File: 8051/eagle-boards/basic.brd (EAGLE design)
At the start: 65.7 x 76.2 mm, 29 parts, among them IC1 AT89S51-24P, IC2 ULN2003AN, IC3 ULN2003AN, Q1 12M

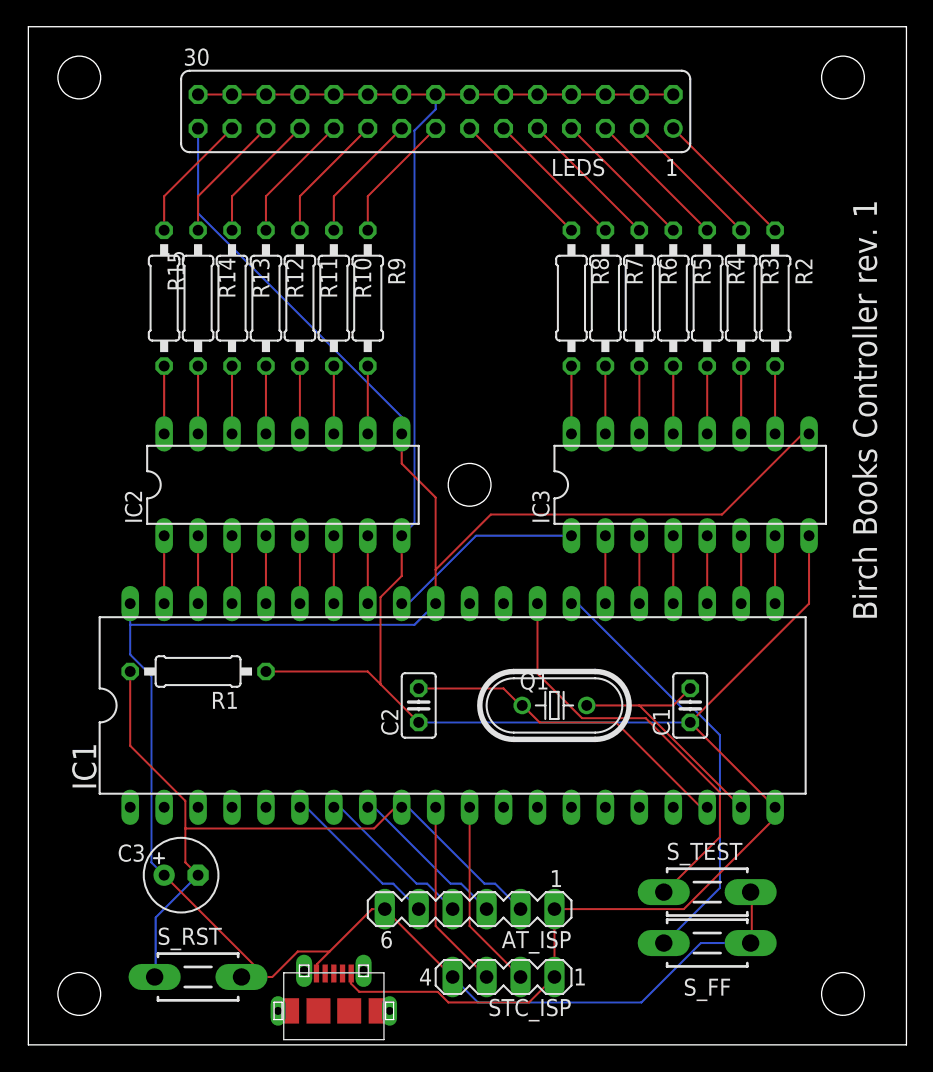
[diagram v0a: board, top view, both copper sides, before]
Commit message: Split the actuation into its own board.
Note that the previous design was broken, as the Darlingtons weren't being grounded, but rather joined to Vcc.
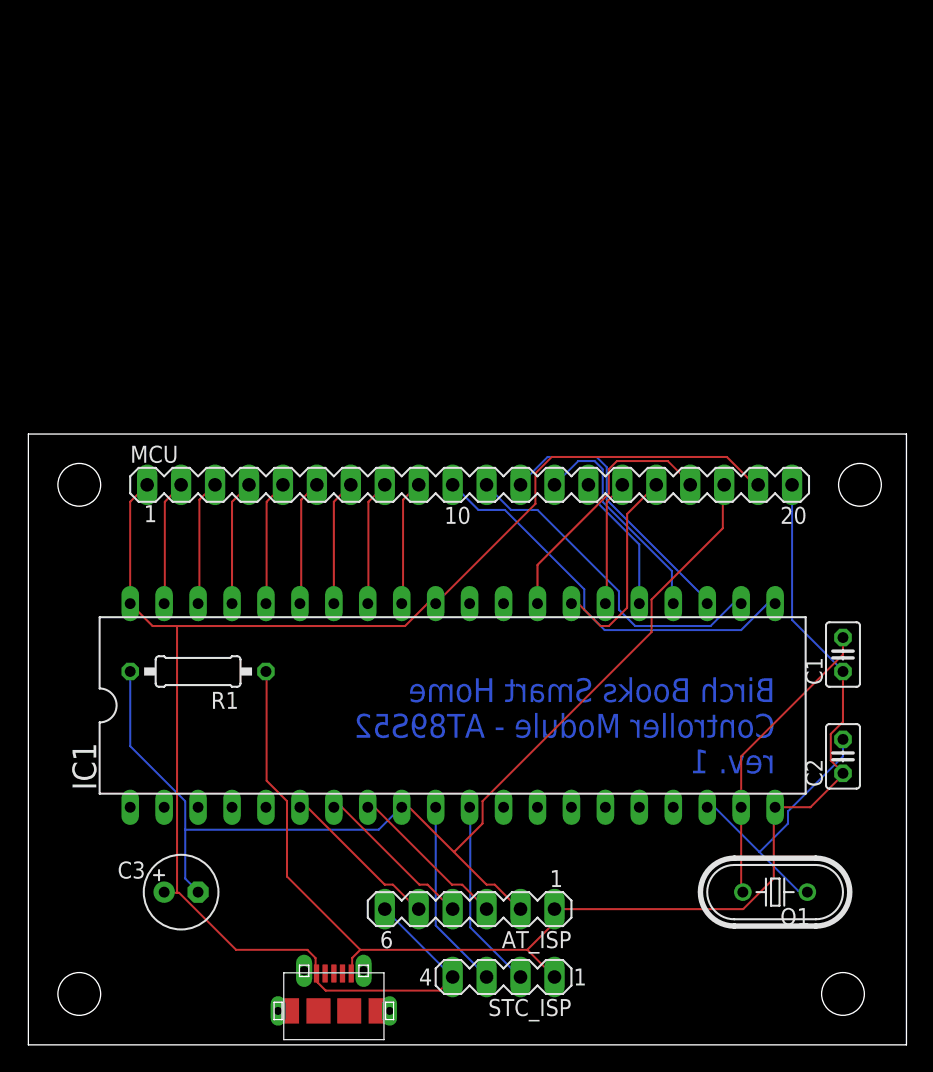
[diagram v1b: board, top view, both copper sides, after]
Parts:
- removed IC2, IC3: ULN2003AN, uln-udn:DIL16
- removed LEDS: (no value), con-lsta:FE15-2
- removed R10, R11, R12, R13, R14, R15, R2, R3, R4, R5, R6, R7, R8, R9: 47, rcl:0207/10
- removed S_FF, S_RST, S_TEST: DTS-3, switch-tact:DTS-3
- added MCU: (no value), con-lstb:MA20-1
- moved C2 32.0 mm to (61.0, 19.1)
- moved Q1 21.6 mm to (55.9, 8.89), turned to 180 degrees
- moved C1 12.0 mm to (61.0, 26.7)
- moved C3 1.27 mm to (11.4, 8.89)
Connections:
- removed net N$21: IC3.11, R3.2
- removed net N$22: IC3.12, R4.2
- removed net N$23: IC3.13, R5.2
- removed net N$24: IC3.14, R6.2
- removed net N$25: IC3.15, R7.2
- removed net N$26: IC3.16, R8.2
- removed net N$27: IC2.10, R9.2
- removed net N$28: IC2.11, R10.2
- removed net N$29: IC2.12, R11.2
- removed net N$30: IC2.13, R12.2
- removed net N$31: IC2.14, R13.2
- removed net N$32: IC2.15, R14.2
- removed net N$33: IC2.16, R15.2
- removed net N$34: LEDS.27, R15.1
- removed net N$35: LEDS.25, R14.1
- removed net N$36: LEDS.23, R13.1
- removed net N$37: LEDS.21, R12.1
- removed net N$38: LEDS.19, R11.1
- removed net N$39: LEDS.17, R10.1
- removed net N$40: LEDS.15, R9.1
- removed net N$41: LEDS.13, R8.1
- removed net N$42: LEDS.11, R7.1
- removed net N$43: LEDS.9, R6.1
- removed net N$44: LEDS.7, R5.1
- removed net N$45: LEDS.5, R4.1
- removed net N$46: LEDS.3, R3.1
- removed net N$47: LEDS.1, R2.1
- removed net N$48: IC1.28, S_TEST.1
- net GND: now also MCU.20; no longer IC2.8, IC3.8, LEDS.10, LEDS.12, LEDS.14, LEDS.16, LEDS.18, LEDS.2, LEDS.20, LEDS.22, LEDS.24, LEDS.26, LEDS.28, LEDS.30, LEDS.4, LEDS.6, LEDS.8
- net N$1: now also IC1.39, MCU.2; no longer IC1.21, IC3.7
- net N$10: now also IC1.33, MCU.8; no longer IC1.35, IC2.5
- net N$11: now also IC1.32, MCU.9; no longer IC1.34, IC2.6
- net N$12: now also IC1.21, MCU.10; no longer IC1.33, IC2.7
- net N$13: now also IC1.22, MCU.11; no longer IC1.32, IC3.1
- net N$14: now also MCU.12; no longer IC3.5
- net N$15: now also MCU.13; no longer IC3.4
- net N$16: now also MCU.14; no longer IC3.3
- net N$17: now also MCU.15; no longer IC3.2
- net N$19: now also MCU.16; no longer S_FF.1
- net N$2: now also IC1.38, MCU.3; no longer IC1.22, IC3.6
- net N$20: now also IC1.28, MCU.17; no longer IC3.10, R2.2
- net N$5: now also MCU.18; no longer S_RST.1
- net N$6: now also IC1.37, MCU.4; no longer IC1.39, IC2.1
- net N$7: now also IC1.36, MCU.5; no longer IC1.38, IC2.2
- net N$8: now also IC1.35, MCU.6; no longer IC1.37, IC2.3
- net N$9: now also IC1.34, MCU.7; no longer IC1.36, IC2.4
- net VCC: now also MCU.1, MCU.19; no longer IC2.9, IC3.9, LEDS.29, S_FF.2, S_RST.2, S_TEST.2
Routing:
- net GND: track 183.9 -> 98.0 mm
- net VCC: track 181.7 -> 117.8 mm
- net N$48: track 31.8 -> 0.00 mm
- net N$5: track 55.3 -> 83.4 mm
- net N$12: track 5.08 -> 30.3 mm
- net N$19: track 32.5 -> 15.5 mm
- net N$14: track 5.08 -> 21.0 mm
- net N$20: track 5.08 -> 19.4 mm
- net N$15: track 5.08 -> 16.9 mm
- net N$47: track 10.8 -> 0.00 mm
- net N$46: track 10.8 -> 0.00 mm
- net N$45: track 10.8 -> 0.00 mm
- net N$44: track 10.8 -> 0.00 mm
- net N$43: track 10.8 -> 0.00 mm
- net N$42: track 10.8 -> 0.00 mm
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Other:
- board size 65.7 x 76.2 mm -> 65.7 x 45.7 mm
- board text added: "Birch Books Smart Home Controller Module - AT89S52 rev. 1"
- board text removed: "Birch Books Controller rev. 1"

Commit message: Fix significant mistakes in the controller board.
The capacitors to stabilise the crystal need to be a bit beefier, make space for them.

Replace the pin header with a female header for the connection to the actuator board.

Necessary: add a resistor network between P0 and the connector.

P0 is the only port needing pull-up resistors.
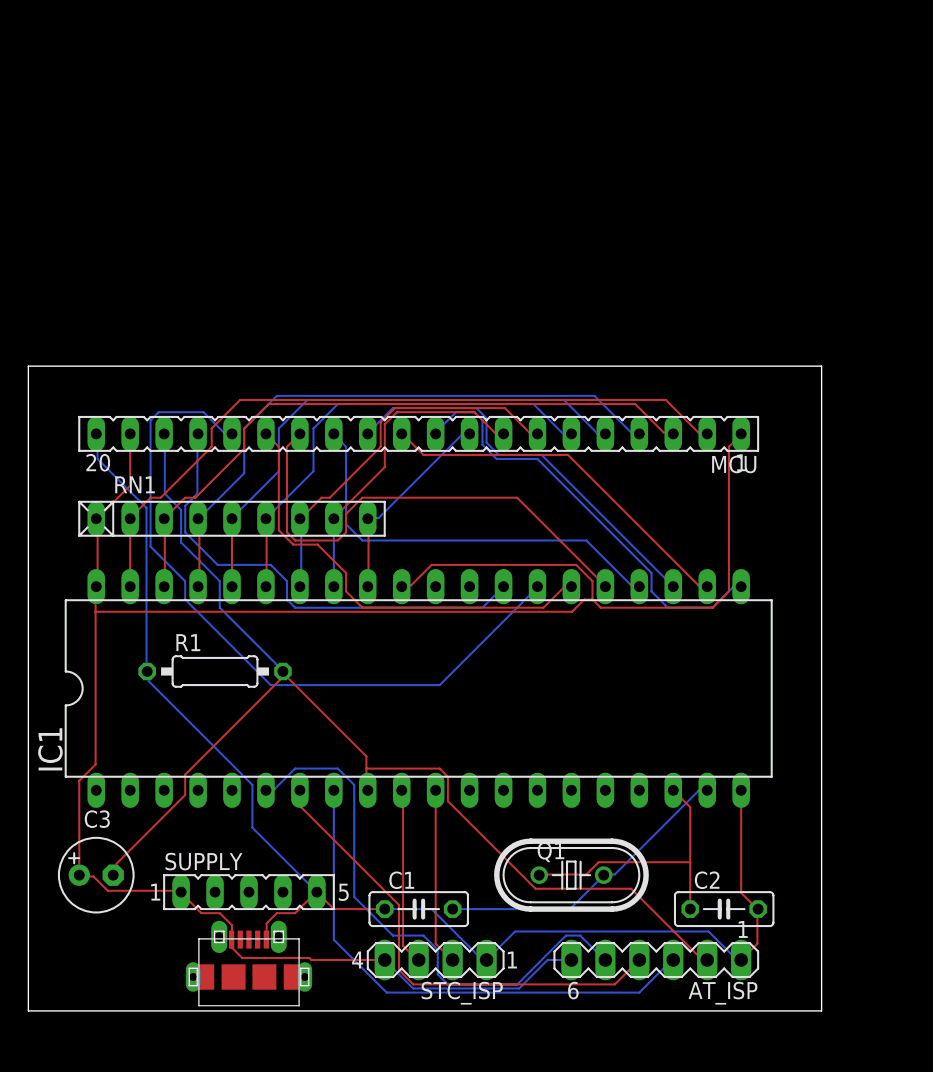
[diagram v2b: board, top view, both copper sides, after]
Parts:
- added RN1: 10k, resistor-net:RN-9
- added SUPPLY: (no value), con-lsta:FE05-1
- C1, C2: value 22p -> 50pF; device rcl:C025-025X050 -> rcl:C050-025X075
- MCU: device con-lstb:MA20-1 -> con-lsta:FE20
- moved C1 37.0 mm to (29.2, 7.62), turned to 0 degrees
- moved Q1 15.3 mm to (40.6, 10.2), turned to 0 degrees
- moved C2 14.5 mm to (52.1, 7.62), turned to 180 degrees
- moved AT_ISP 14.5 mm to (47.0, 3.81)
- moved U$1 6.84 mm to (16.5, 2.54)
- moved C3 6.48 mm to (5.08, 10.2)
- moved MCU 5.39 mm to (29.2, 43.2), turned to 180 degrees
- moved STC_ISP 5.24 mm to (30.5, 3.81)
- moved IC1 2.84 mm to (29.2, 24.1)
- moved R1 1.27 mm to (14.0, 25.4), turned to 0 degrees
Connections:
- removed net N$1: IC1.39, MCU.2
- removed net N$2 (its old number): IC1.38, MCU.3
- removed net N$6 (its old number): IC1.37, MCU.4
- removed net N$8 (its old number): IC1.35, MCU.6
- removed net N$9 (its old number): IC1.34, MCU.7
- new net N$12: IC1.34, MCU.7, RN1.7
- new net N$13: IC1.33, MCU.8, RN1.8
- new net N$14: IC1.32, MCU.9, RN1.9
- new net N$22: IC1.37, MCU.4, RN1.4
- new net N$26: IC1.39, MCU.2, RN1.2
- net GND: now also SUPPLY.5
- net N$10: now also IC1.36, MCU.5, RN1.5; no longer IC1.33, MCU.8
- net N$11: now also IC1.35, MCU.6, RN1.6; no longer IC1.32, MCU.9
- net N$7: now also IC1.38, MCU.3, RN1.3; no longer IC1.36, MCU.5
- net VCC: now also RN1.1, SUPPLY.1
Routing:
- net N$26: track 0.00 -> 53.8 mm
- net N$22: track 0.00 -> 45.2 mm
- net N$7: track 9.45 -> 48.6 mm
- net N$6: track 15.5 -> 53.7 mm
- net VCC: track 117.8 -> 154.6 mm
- net N$10: track 9.45 -> 39.7 mm
- net N$51: track 12.0 -> 41.0 mm
- net N$12: track 0.00 -> 28.3 mm
- net N$49: track 12.0 -> 39.2 mm
- net N$9: track 10.5 -> 36.7 mm
- net N$11: track 9.50 -> 34.3 mm
- net N$8: track 9.52 -> 33.4 mm
- net N$50: track 12.0 -> 35.7 mm
- net N$13: track 0.00 -> 23.7 mm
- net N$2: track 19.4 -> 35.4 mm
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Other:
- board size 65.7 x 45.7 mm -> 59.4 x 48.2 mm
